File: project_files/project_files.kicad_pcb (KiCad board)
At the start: 2 copper layers, 95.3 x 104.8 mm, 48 parts, among them SW11 SW_Push, SW12 SW_Push, SW13 SW_Push, SW17 SW_Push, SW18 SW_Push, SW19 SW_Push, SW3 SW_Push, SW4 SW_Push, SW5 SW_Push, SW7 SW_Push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

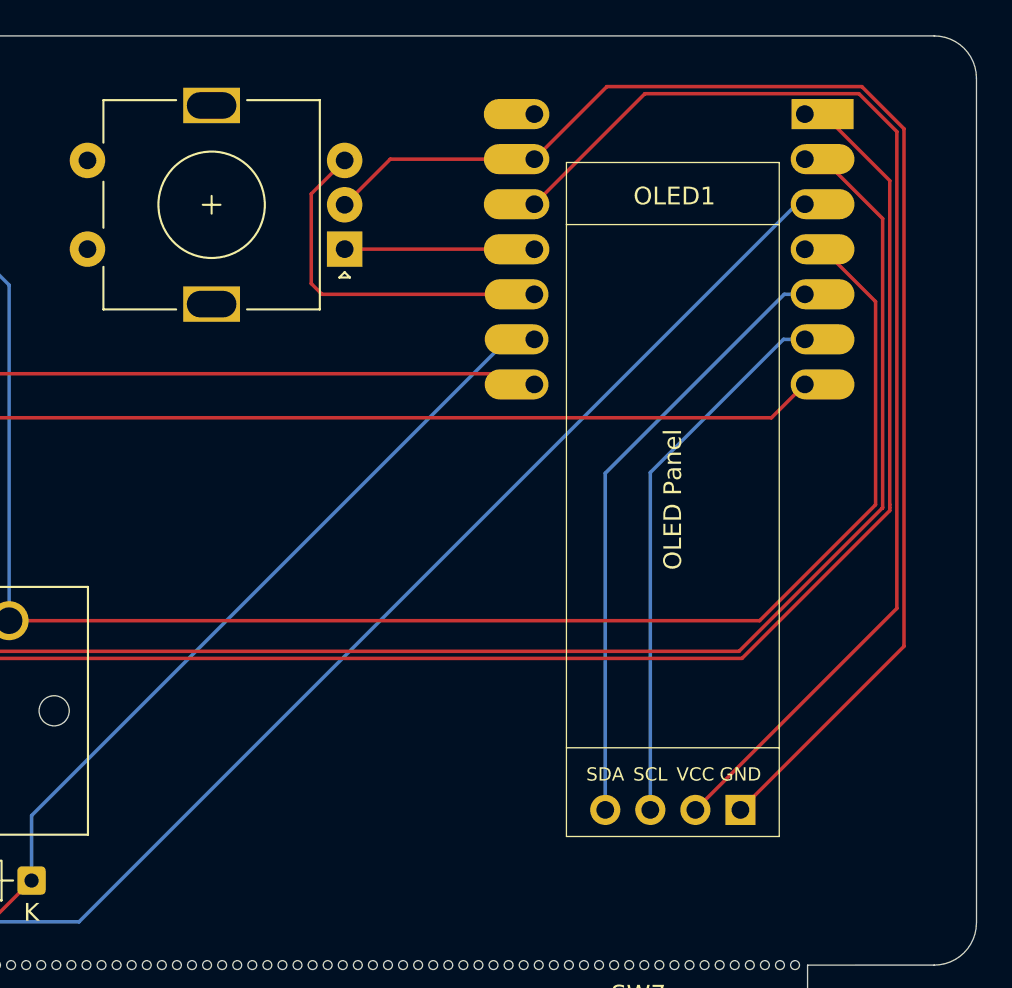
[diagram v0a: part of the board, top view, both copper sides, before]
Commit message: oled centered
with silkscreen!
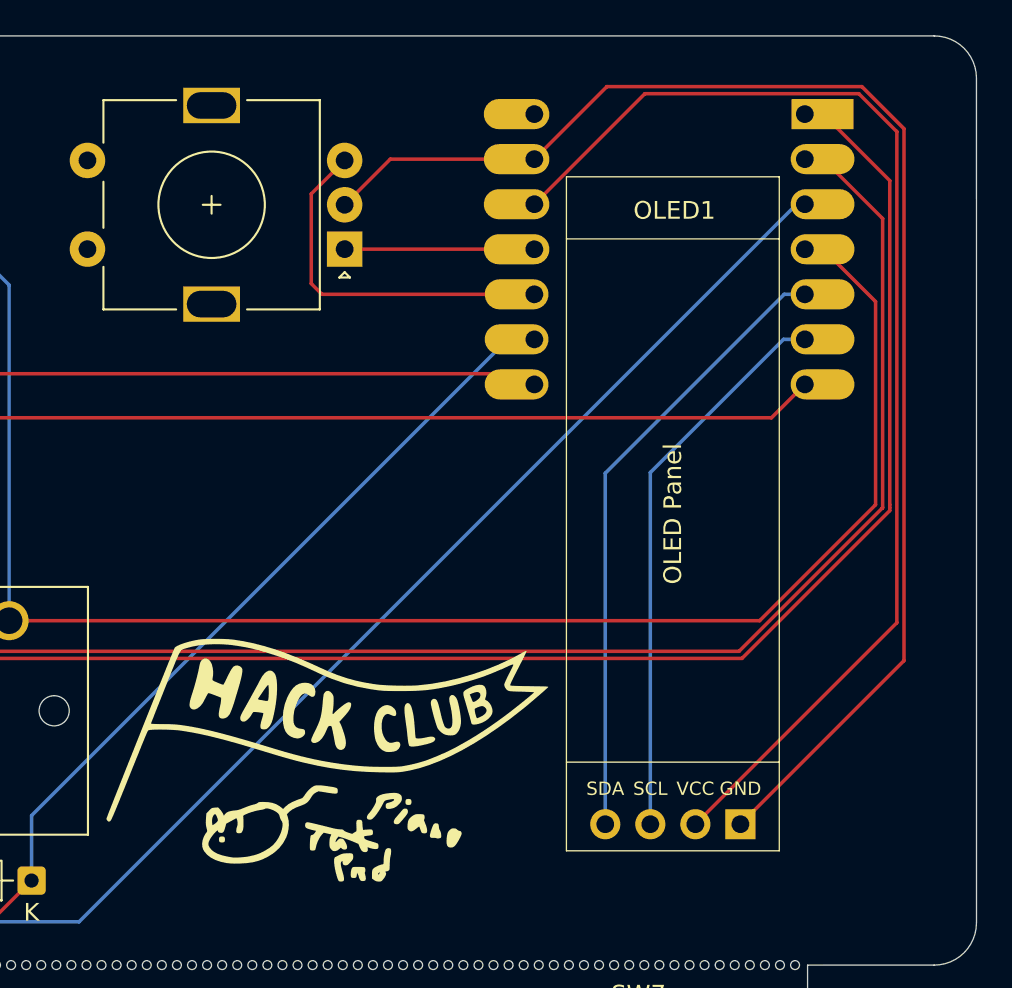
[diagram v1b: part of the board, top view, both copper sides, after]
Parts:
- added ?: LOGO, custom:silkscreen, F.Cu at (153.6, 79.8)
- moved OLED1 0.81 mm to (179.4, 46.0)
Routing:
- net GND: track 77.5 -> 78.3 mm
- net /PWR_3v3: track 66.8 -> 67.7 mm

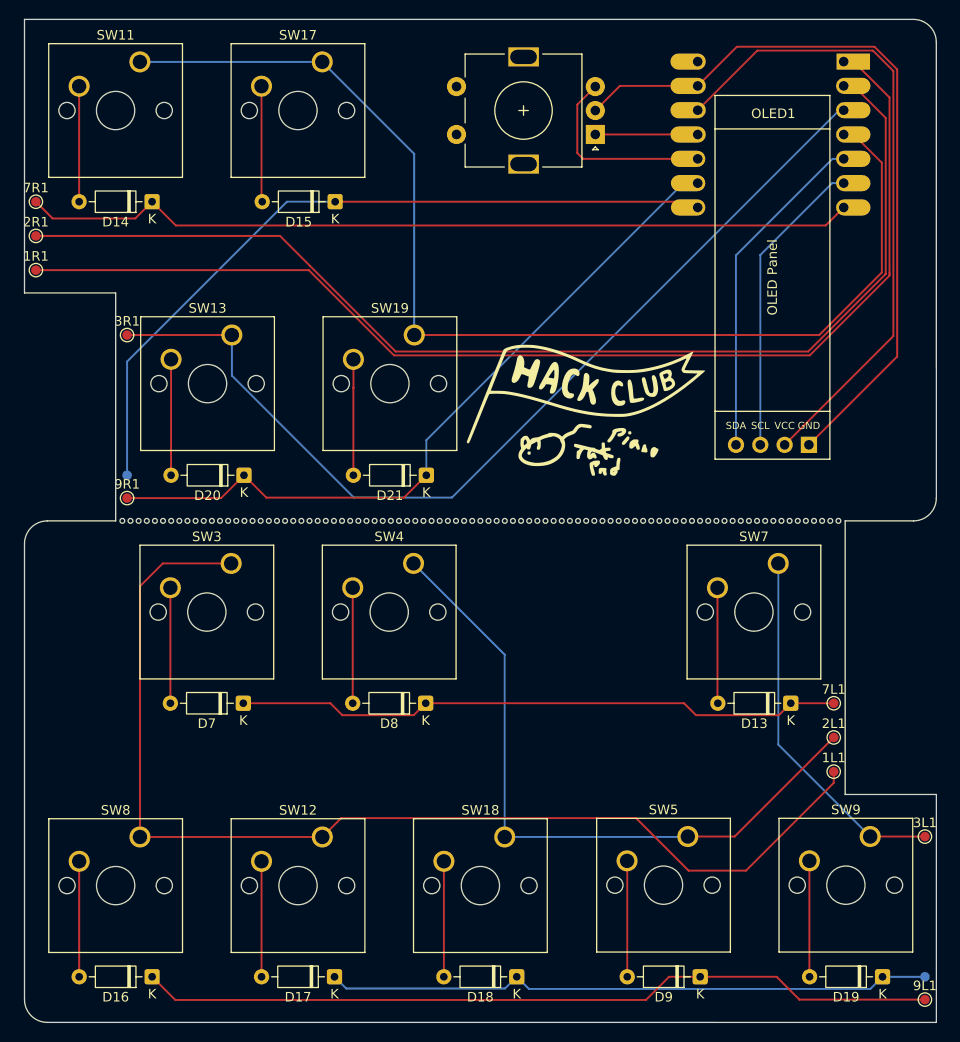
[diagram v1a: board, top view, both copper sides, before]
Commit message: lots of case work
pcb subject to change, so no gerbers yet
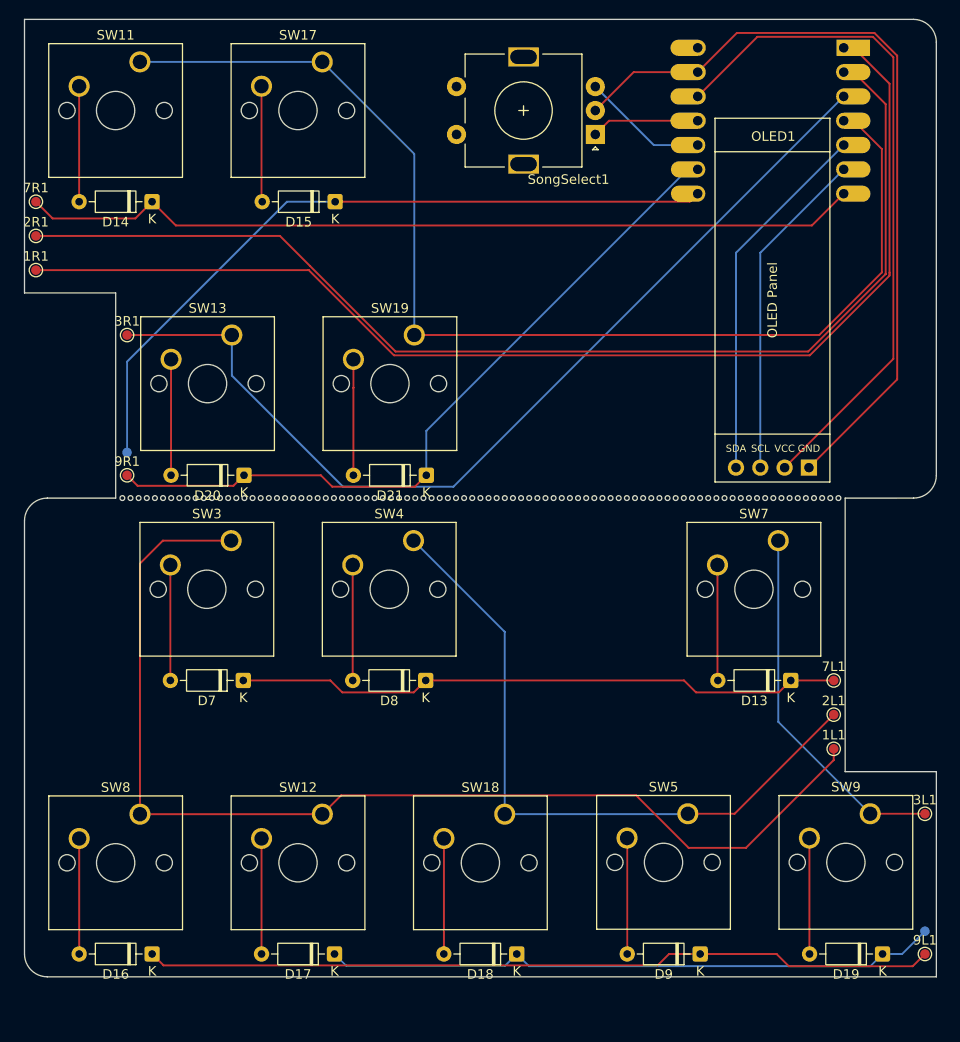
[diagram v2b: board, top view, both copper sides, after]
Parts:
- removed ?: LOGO, custom:silkscreen
- SW11, SW12, SW13, SW17, SW18, SW19, SW3, SW4, SW5, SW7, SW8, SW9: footprint Button_Switch_Keyboard:SW_Cherry_MX_1.00u_PCB -> custom:SW_Cherry_MX_1.00u_PCB
- SongSelect1: footprint Rotary_Encoder:RotaryEncoder_Alps_EC11E-Switch_Vertical_H20mm -> custom:RotaryEncoder_Alps_EC11E-Switch_Vertical_H20mm
- moved 8L1 4.76 mm to (189.3, 133.3)
- moved 9L1 4.76 mm to (189.3, 135.7)
- moved 3L1 2.38 mm to (189.3, 121.1)
- moved 9R1 2.38 mm to (106.0, 85.7)
- moved SW3 2.38 mm to (116.8, 92.5)
- moved SW4 2.38 mm to (135.9, 92.5)
- moved SW7 2.38 mm to (174.0, 92.5)
- moved 1L1 2.38 mm to (179.8, 114.3)
- moved 2L1 2.38 mm to (179.8, 110.7)
- moved 7L1 2.38 mm to (179.8, 107.2)
- moved D13 2.38 mm to (175.3, 107.2)
- moved D16 2.38 mm to (108.6, 135.7)
- moved D17 2.38 mm to (127.6, 135.7)
- moved D18 2.38 mm to (146.7, 135.7)
- moved D19 2.38 mm to (184.9, 135.7)
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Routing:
- net /PIN_10: track 20.5 -> 13.2 mm
- net GND: track 78.3 -> 82.7 mm
- net /SDA: track 34.4 -> 38.4 mm
- net /SCL: track 30.8 -> 34.8 mm
- net /PWR_3v3: track 67.7 -> 71.5 mm
- net /PIN_1: track 237.5 -> 238.9 mm
- net /PIN_4: track 118.7 -> 120.2 mm
- net /PIN_2: track 189.3 -> 190.7 mm
- net /PIN_11: track 10.7 -> 11.3 mm
- net /PIN_7: track 151.4 -> 152.0 mm
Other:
- board size 95.3 x 104.8 mm -> 95.3 x 100 mm
